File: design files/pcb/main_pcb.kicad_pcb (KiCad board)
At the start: 2 copper layers, 29 x 99 mm, 28 parts, among them CN1 MCP4725-B, P1 PWR, Q1 BC547A, Q2 BC547A, U1 MCP6002-EP, U3 7805

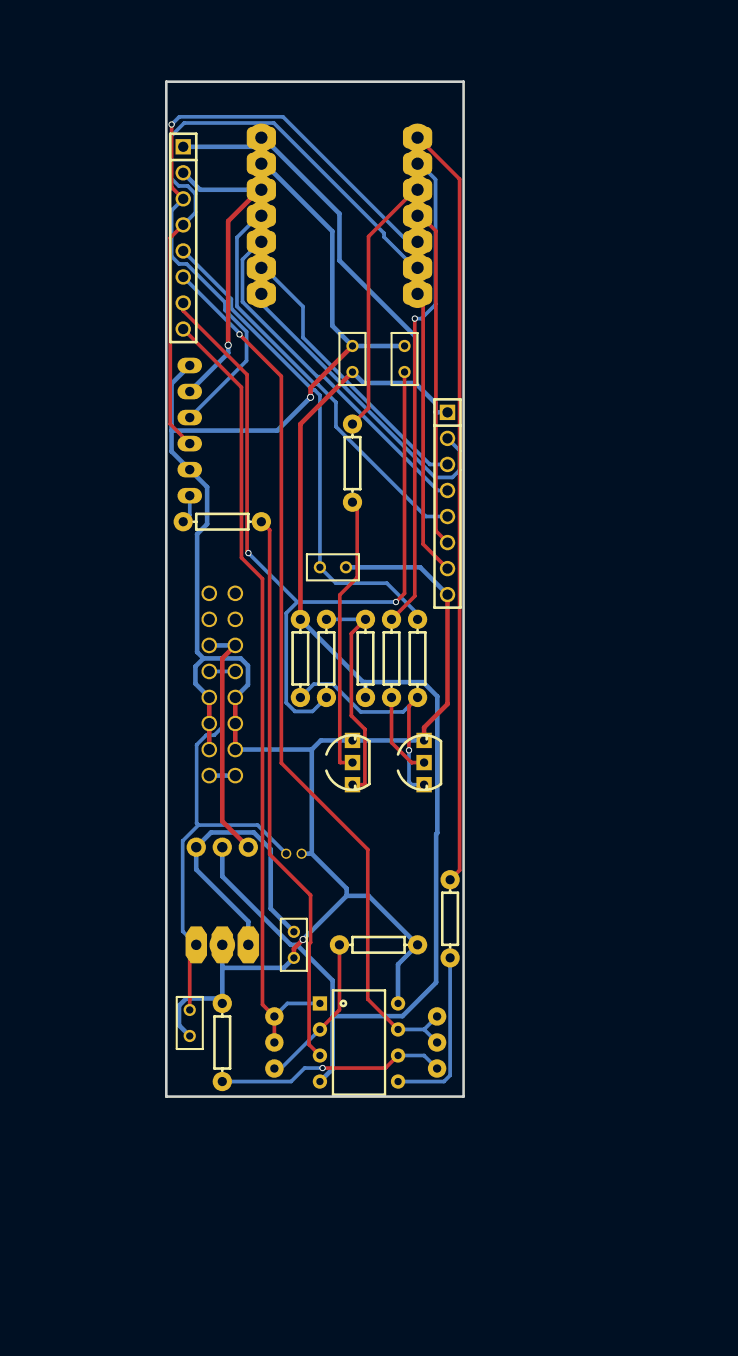
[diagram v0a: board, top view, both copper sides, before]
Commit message: fixed orientation for mcp6002
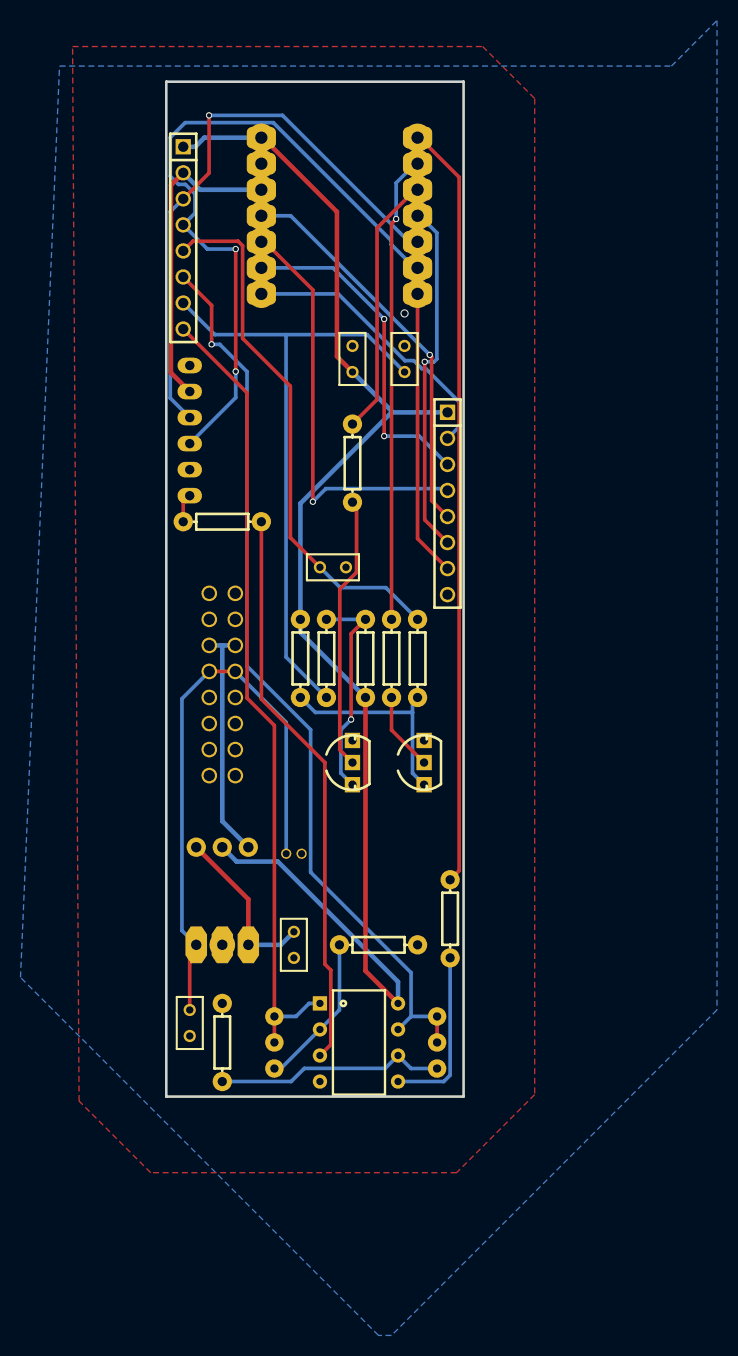
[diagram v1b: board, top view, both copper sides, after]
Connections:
- P1 pad 1: -12V -> (no net)
- P1 pad 2: -12V -> (no net)
- U1 pad 4: 5V -> GND
- U1 pad 8: GND -> 5V
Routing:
- net GND: track 209.1 -> 0.00 mm, vias 2 -> 1
- net 5V: track 161.5 -> 135.6 mm
- net O3_CON: track 81.3 -> 61.4 mm, vias 2 -> 0
- net REG_5: track 29.1 -> 16.6 mm
- net P1_10: track 48.3 -> 57.3 mm
- net SDA: track 64.6 -> 57.3 mm
- net IN_3: track 34.3 -> 41.4 mm, vias 0 -> 1
- net IN_2: track 27.9 -> 32.8 mm, vias 0 -> 2
- net SCL: track 63.9 -> 68.1 mm, vias 0 -> 2
- net O1_CON: track 48.4 -> 52.5 mm
- net IN_1: track 31.2 -> 27.7 mm
- net Q1_1: track 23.8 -> 20.7 mm, vias 1 -> 0
- net -12V: track 2.54 -> 0.00 mm
- net ENC_SW: track 40.4 -> 38.5 mm, vias 0 -> 1
- net O1: track 47.5 -> 45.6 mm
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- added copper zone on B.Cu, net GND
- added copper zone on F.Cu, net GND
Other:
- board text added: "CIRCUIT BY HAGWO"
- board text added: "HAGIWO QUANTIZER/SH101"
- board text added: "PCB BY TESTBILD"
- board text added: "SEQUENCER 1.1"
- board text added: "XIAO SAMD21"
- board text removed: "XIAO"
